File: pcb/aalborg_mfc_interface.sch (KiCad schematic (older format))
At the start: 31 parts, among them J1 DB15FV, J2 DB15FV, J3 DB15FV, P1 PWR_JACK_2.5x5.5, P2 HEADER_01X03, P3 HEADER_01X03_SHR, P4 HEADER_01X03_SHR, P5 HEADER_01X03_SHR, SW1 SPST_SERIES_M, SW2 KT_SWITCH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

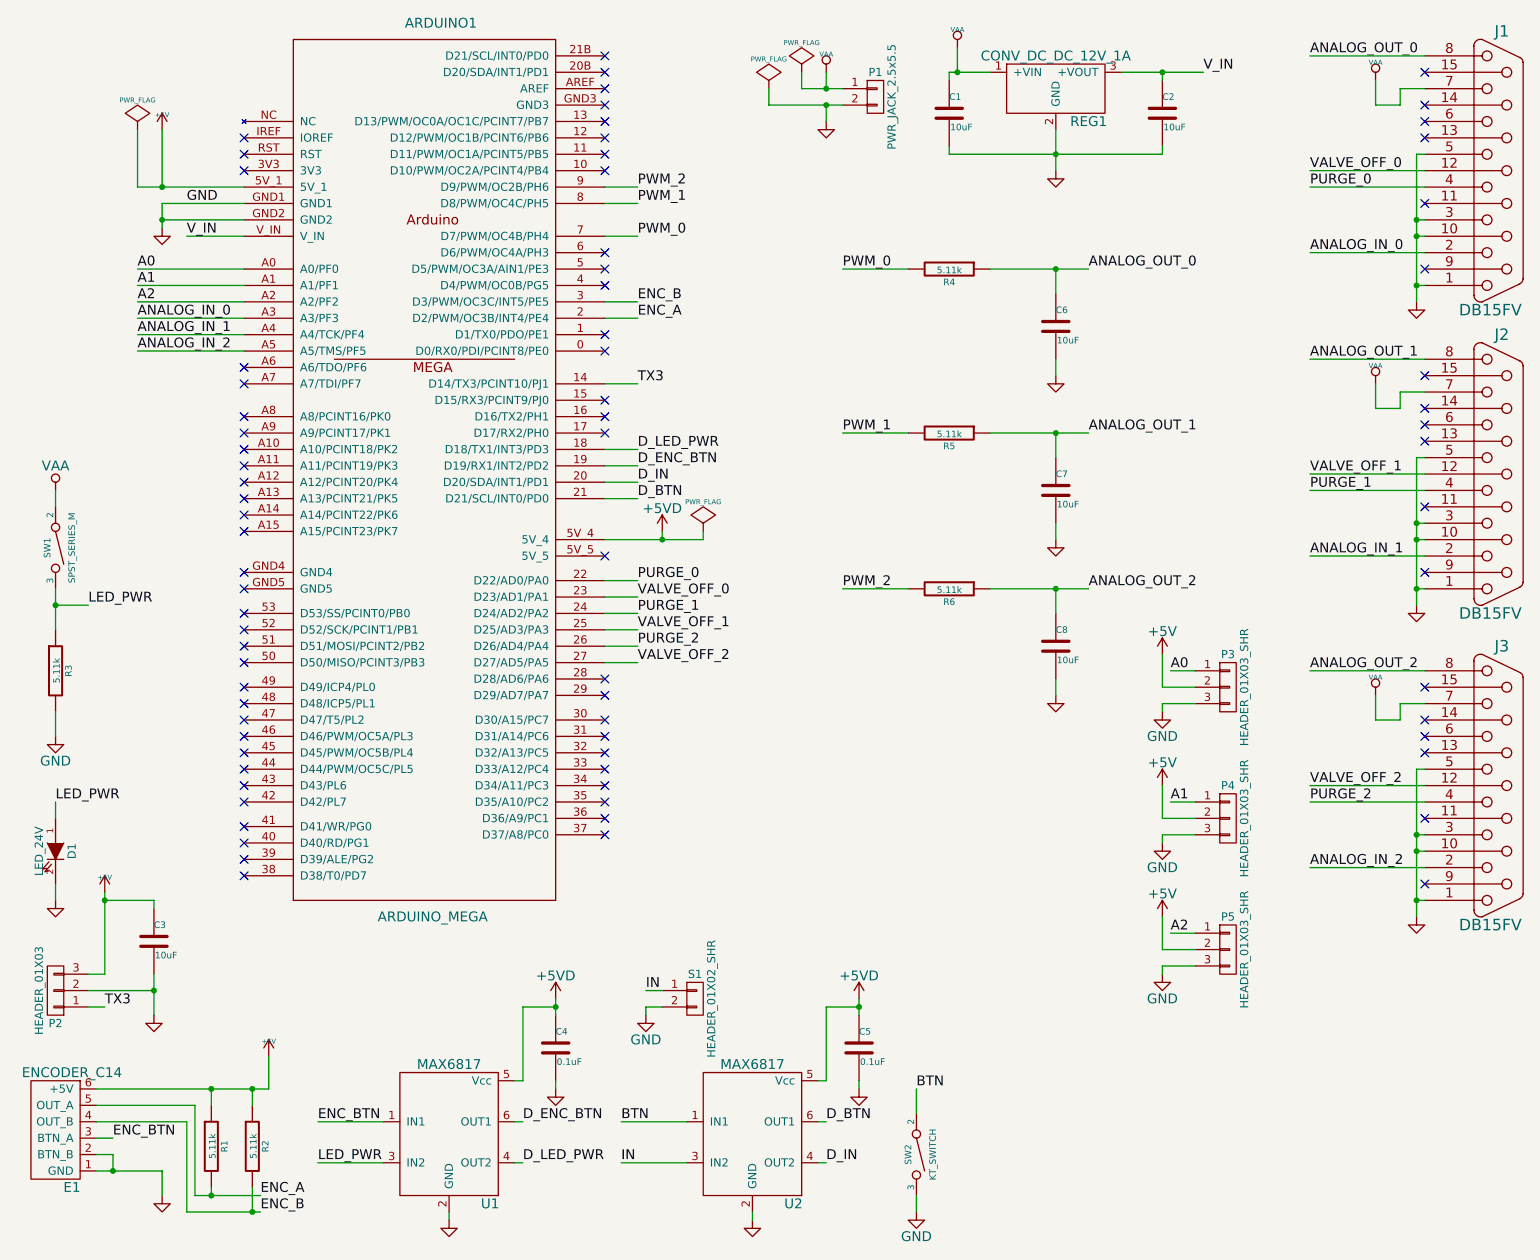
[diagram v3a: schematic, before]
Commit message: Added StandAlone frames.
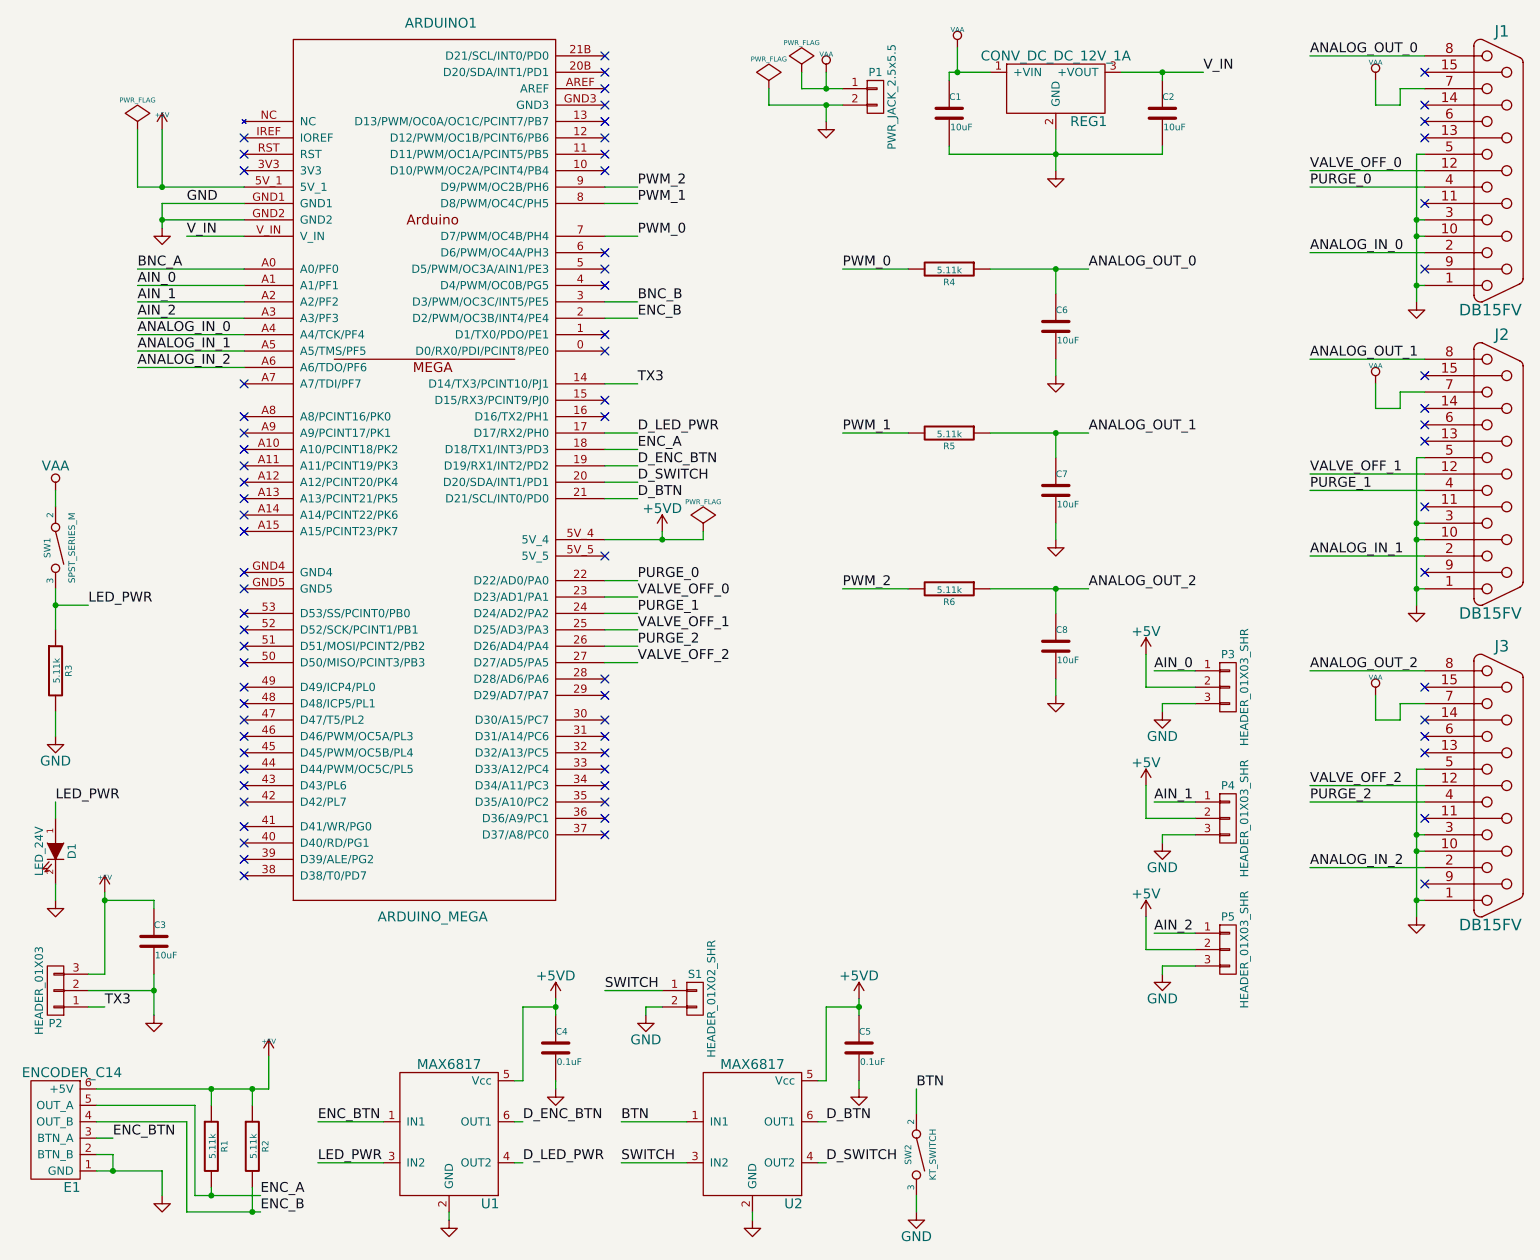
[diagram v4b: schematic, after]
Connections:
- net ANALOG_IN_0: now also ARDUINO1.A4 (A4/TCK/PF4); no longer ARDUINO1.A3 (A3/PF3)
- net ANALOG_IN_1: now also ARDUINO1.A5 (A5/TMS/PF5); no longer ARDUINO1.A4 (A4/TCK/PF4)
- net ANALOG_IN_2: now also ARDUINO1.A6 (A6/TDO/PF6); no longer ARDUINO1.A5 (A5/TMS/PF5)
- net D_LED_PWR: now also ARDUINO1.17 (D17/RX2/PH0); no longer ARDUINO1.18 (D18/TX1/INT3/PD3)
- net ENC_A: now also ARDUINO1.18 (D18/TX1/INT3/PD3); no longer ARDUINO1.2 (D2/PWM/OC3B/INT4/PE4)
- net ENC_B: now also ARDUINO1.2 (D2/PWM/OC3B/INT4/PE4); no longer ARDUINO1.3 (D3/PWM/OC3C/INT5/PE5)
- net A0 renamed AIN_0
- net AIN_0: now also ARDUINO1.A1 (A1/PF1); no longer ARDUINO1.A0 (A0/PF0)
- net A1 renamed AIN_1
- net AIN_1: now also ARDUINO1.A2 (A2/PF2); no longer ARDUINO1.A1 (A1/PF1)
- net A2 renamed AIN_2
- net AIN_2: now also ARDUINO1.A3 (A3/PF3); no longer ARDUINO1.A2 (A2/PF2)
- net D_IN renamed D_SWITCH
- net IN renamed SWITCH
- new net BNC_A: ARDUINO1.A0 (A0/PF0)
- new net BNC_B: ARDUINO1.3 (D3/PWM/OC3C/INT5/PE5)
- no-connect marks 76 -> 74
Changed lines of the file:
@@
 LIBS:valves
 LIBS:aalborg_mfc_interface
-LIBS:components
 LIBS:aalborg_mfc_interface-cache
 EELAYER 25 0
@@
 Title "aalborg_mfc_interface"
 Date ""
-Rev "1.1"
+Rev "1.2"
 Comp "Janelia"
 Comment1 ""
@@
 	1850 1750 1350 1750
 Connection ~ 1350 1750
-NoConn ~ 1850 2650
 NoConn ~ 1850 2750
 NoConn ~ 1850 2950
@@
 NoConn ~ 4050 2850
 NoConn ~ 4050 2950
-NoConn ~ 4050 3050
 NoConn ~ 4050 3800
 NoConn ~ 4050 4550
@@
 	4050 2350 4250 2350
 Text Label 4250 2350 0    60   ~ 0
-ENC_A
+ENC_B
 Wire Wire Line
 	4050 2250 4250 2250
 Text Label 4250 2250 0    60   ~ 0
-ENC_B
+BNC_B
 Wire Wire Line
 	1050 7450 1050 7550
@@
 Text Label 8350 1950 0    60   ~ 0
 ANALOG_IN_0
-Text Label 1200 2350 0    60   ~ 0
+Text Label 1200 2450 0    60   ~ 0
 ANALOG_IN_0
-Text Label 1200 2450 0    60   ~ 0
+Text Label 1200 2550 0    60   ~ 0
 ANALOG_IN_1
 Wire Wire Line
@@
 Wire Wire Line
 	4050 3150 4250 3150
-Text Label 4250 3150 0    60   ~ 0
+Text Label 4250 3050 0    60   ~ 0
 D_LED_PWR
 Text Label 700  5300 0    60   ~ 0
@@
 Wire Wire Line
 	1850 2350 1200 2350
-Text Label 1200 2550 0    60   ~ 0
+Text Label 1200 2650 0    60   ~ 0
 ANALOG_IN_2
 NoConn ~ 4050 1450
@@
 Wire Wire Line
 	1850 2550 1200 2550
-Text Label 1200 2050 0    60   ~ 0
-A0
 Text Label 1200 2150 0    60   ~ 0
-A1
+AIN_0
 Text Label 1200 2250 0    60   ~ 0
-A2
-Wire Wire Line
-	7650 4500 7500 4500
-Text Label 7500 4500 0    60   ~ 0
-A0
+AIN_1
+Text Label 1200 2350 0    60   ~ 0
+AIN_2
+Wire Wire Line
+	7650 4500 7400 4500
+Text Label 7400 4500 0    60   ~ 0
+AIN_0
 $Comp
 L +5V #PWR028
 U 1 1 54B5A3F5
-P 7450 4400
-F 0 "#PWR028" H 7450 4250 60  0001 C CNN
-F 1 "+5V" H 7450 4540 60  0000 C CNN
-F 2 "" H 7450 4400 60  0000 C CNN
-F 3 "" H 7450 4400 60  0000 C CNN
-	1    7450 4400
+P 7350 4400
+F 0 "#PWR028" H 7350 4250 60  0001 C CNN
+F 1 "+5V" H 7350 4540 60  0000 C CNN
+F 2 "" H 7350 4400 60  0000 C CNN
+F 3 "" H 7350 4400 60  0000 C CNN
+	1    7350 4400
 	1    0    0    -1
 $EndComp
@@
 $EndComp
 Wire Wire Line
-	7650 4600 7450 4600
-Wire Wire Line
-	7450 4600 7450 4400
-Wire Wire Line
 	7650 4700 7450 4700
 Wire Wire Line
 	7450 4700 7450 4750
 Wire Wire Line
-	7650 5300 7500 5300
-Text Label 7500 5300 0    60   ~ 0
-A1
+	7650 5300 7400 5300
+Text Label 7400 5300 0    60   ~ 0
+AIN_1
 $Comp
 L +5V #PWR030
 U 1 1 54B5A9BF
-P 7450 5200
-F 0 "#PWR030" H 7450 5050 60  0001 C CNN
-F 1 "+5V" H 7450 5340 60  0000 C CNN
-F 2 "" H 7450 5200 60  0000 C CNN
-F 3 "" H 7450 5200 60  0000 C CNN
-	1    7450 5200
+P 7350 5200
+F 0 "#PWR030" H 7350 5050 60  0001 C CNN
+F 1 "+5V" H 7350 5340 60  0000 C CNN
+F 2 "" H 7350 5200 60  0000 C CNN
+F 3 "" H 7350 5200 60  0000 C CNN
+	1    7350 5200
 	1    0    0    -1
 $EndComp
@@
 $EndComp
 Wire Wire Line
-	7650 5400 7450 5400
-Wire Wire Line
-	7450 5400 7450 5200
-Wire Wire Line
 	7650 5500 7450 5500
 Wire Wire Line
 	7450 5500 7450 5550
 Wire Wire Line
-	7650 6100 7500 6100
-Text Label 7500 6100 0    60   ~ 0
-A2
+	7650 6100 7400 6100
+Text Label 7400 6100 0    60   ~ 0
+AIN_2
 $Comp
 L +5V #PWR032
 U 1 1 54B5AB98
-P 7450 6000
-F 0 "#PWR032" H 7450 5850 60  0001 C CNN
-F 1 "+5V" H 7450 6140 60  0000 C CNN
-F 2 "" H 7450 6000 60  0000 C CNN
-F 3 "" H 7450 6000 60  0000 C CNN
-	1    7450 6000
+P 7350 6000
+F 0 "#PWR032" H 7350 5850 60  0001 C CNN
+F 1 "+5V" H 7350 6140 60  0000 C CNN
+F 2 "" H 7350 6000 60  0000 C CNN
+F 3 "" H 7350 6000 60  0000 C CNN
+	1    7350 6000
 	1    0    0    -1
 $EndComp
@@
 	1    0    0    -1
 $EndComp
-Wire Wire Line
-	7650 6200 7450 6200
-Wire Wire Line
-	7450 6200 7450 6000
 Wire Wire Line
 	7650 6300 7450 6300
@@
 	4550 7500 4150 7500
 Text Label 4150 7500 0    60   ~ 0
-IN
+SWITCH
 Wire Wire Line
 	5350 7500 5400 7500
 Text Label 5400 7500 0    60   ~ 0
-D_IN
+D_SWITCH
 $Comp
 L +5VD #PWR039
@@
 Connection ~ 5600 6550
 Wire Wire Line
-	4400 6450 4300 6450
-Text Label 4300 6450 0    60   ~ 0
-IN
+	4400 6450 4050 6450
+Text Label 4050 6450 0    60   ~ 0
+SWITCH
 $Comp
 L GND #PWR040
@@
 D_BTN
 Text Label 4250 3350 0    60   ~ 0
-D_IN
+D_SWITCH
 $Comp
 L GND #PWR041
@@
 	1    0    0    -1
 $EndComp
+Wire Wire Line
+	4050 3050 4250 3050
+Text Label 4250 3150 0    60   ~ 0
+ENC_A
+Wire Wire Line
+	1850 2650 1200 2650
+Text Label 1200 2050 0    60   ~ 0
+BNC_A
+Wire Wire Line
+	7350 4400 7350 4600
+Wire Wire Line
+	7350 4600 7650 4600
+Wire Wire Line
+	7350 5200 7350 5400
+Wire Wire Line
+	7350 5400 7650 5400
+Wire Wire Line
+	7350 6000 7350 6200
+Wire Wire Line
+	7350 6200 7650 6200
 $EndSCHEMATC

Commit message: Finished pcb v1.2.
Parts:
- added P3: BNC_DOUBLE_RA, aalborg_mfc_interface:BNC_DOUBLE, symbol BNC_DOUBLE_RA
- renumbered P3 to P4, P4 to P5, P5 to P6
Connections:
- net BNC_A: now also P3.1 (P1)
- net BNC_B: now also P3.3 (P3)
- net GND: now also P3.2 (P2), P3.4 (P4)
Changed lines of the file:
@@
 	1200 1200 1200 1550
 Wire Wire Line
-	1200 1550 1350 1550
-Wire Wire Line
-	1350 1550 1850 1550
+	1200 1550 1850 1550
 Wire Wire Line
 	1350 1200 1350 1550
@@
 	1850 1650 1350 1650
 Wire Wire Line
-	1350 1650 1350 1750
-Wire Wire Line
-	1350 1750 1350 1800
+	1350 1650 1350 1800
 Wire Wire Line
 	1850 1750 1350 1750
@@
 $EndComp
 Wire Wire Line
-	5250 950  5400 950
-Wire Wire Line
-	5400 950  5500 950
+	5250 950  5500 950
 Wire Wire Line
 	5250 950  5250 850
@@
 Connection ~ 5400 950
 Wire Wire Line
-	5050 1050 5400 1050
-Wire Wire Line
-	5400 1050 5500 1050
+	5050 1050 5500 1050
 Wire Wire Line
 	5050 1050 5050 950
@@
 $EndComp
 Wire Wire Line
-	1300 6350 1300 6450
-Wire Wire Line
-	1300 6450 1300 6600
+	1300 6350 1300 6600
 Wire Wire Line
 	900  6450 1300 6450
@@
 	1300 5900 1000 5900
 Wire Wire Line
-	1000 5850 1000 5900
-Wire Wire Line
-	1000 5900 1000 6350
+	1000 5850 1000 6350
 Wire Wire Line
 	1000 6350 900  6350
@@
 $EndComp
 Wire Wire Line
-	6800 1200 6800 1350
-Wire Wire Line
-	6800 1350 6800 1450
+	6800 1200 6800 1450
 Wire Wire Line
 	6150 1300 6150 1350
 Wire Wire Line
-	6150 1350 6800 1350
-Wire Wire Line
-	6800 1350 7450 1350
+	6150 1350 7450 1350
 Connection ~ 6800 1350
 Wire Wire Line
@@
 	6150 900  6150 850
 Wire Wire Line
-	6150 850  6200 850
-Wire Wire Line
-	6200 850  6400 850
-Wire Wire Line
-	7200 850  7450 850
-Wire Wire Line
-	7450 850  7700 850
+	6150 850  6400 850
+Wire Wire Line
+	7200 850  7700 850
 Wire Wire Line
 	7450 900  7450 850
@@
 $EndComp
 Wire Wire Line
-	950  7550 1050 7550
-Wire Wire Line
-	1050 7550 1350 7550
+	950  7550 1350 7550
 Wire Wire Line
 	1350 7550 1350 7700
@@
 $EndComp
 Wire Wire Line
-	950  7050 1650 7050
-Wire Wire Line
-	1650 7050 1900 7050
-Wire Wire Line
-	1900 7050 2000 7050
+	950  7050 2000 7050
 Wire Wire Line
 	2000 7050 2000 6850
@@
 	1550 7150 1550 7700
 Wire Wire Line
-	1550 7700 1650 7700
-Wire Wire Line
-	1650 7700 1950 7700
+	1550 7700 1950 7700
 Wire Wire Line
 	950  7250 1500 7250
@@
 	1500 7250 1500 7800
 Wire Wire Line
-	1500 7800 1900 7800
-Wire Wire Line
-	1900 7800 1950 7800
+	1500 7800 1950 7800
 Text Label 1050 7350 0    60   ~ 0
 ENC_BTN
@@
 	3750 7000 3750 7050
 Wire Wire Line
-	3750 6500 3750 6550
-Wire Wire Line
-	3750 6550 3750 6600
+	3750 6500 3750 6600
 Wire Wire Line
 	4050 3250 4250 3250
@@
 	9050 1350 9000 1350
 Wire Wire Line
-	9000 1350 9000 1750
-Wire Wire Line
-	9000 1750 9000 1850
-Wire Wire Line
-	9000 1850 9000 2150
-Wire Wire Line
-	9000 2150 9000 2250
+	9000 1350 9000 2250
 Wire Wire Line
 	9050 2150 9000 2150
@@
 	6800 2600 6800 2700
 Wire Wire Line
-	6400 2050 6800 2050
-Wire Wire Line
-	6800 2050 7000 2050
+	6400 2050 7000 2050
 Wire Wire Line
 	6800 2200 6800 2050
@@
 	6800 3600 6800 3700
 Wire Wire Line
-	6400 3050 6800 3050
-Wire Wire Line
-	6800 3050 7000 3050
+	6400 3050 7000 3050
 Wire Wire Line
 	6800 3200 6800 3050
@@
 	9050 3200 9000 3200
 Wire Wire Line
-	9000 3200 9000 3600
-Wire Wire Line
-	9000 3600 9000 3700
-Wire Wire Line
-	9000 3700 9000 4000
-Wire Wire Line
-	9000 4000 9000 4100
+	9000 3200 9000 4100
 Wire Wire Line
 	9050 4000 9000 4000
@@
 $EndComp
 Wire Wire Line
-	700  4000 700  4100
-Wire Wire Line
-	700  4100 700  4250
+	700  4000 700  4250
 Wire Wire Line
 	700  4750 700  4900
@@
 	9050 5100 9000 5100
 Wire Wire Line
-	9000 5100 9000 5500
-Wire Wire Line
-	9000 5500 9000 5600
-Wire Wire Line
-	9000 5600 9000 5900
-Wire Wire Line
-	9000 5900 9000 6000
+	9000 5100 9000 6000
 Wire Wire Line
 	9050 5900 9000 5900
@@
 	6800 4550 6800 4650
 Wire Wire Line
-	6400 4000 6800 4000
-Wire Wire Line
-	6800 4000 7000 4000
+	6400 4000 7000 4000
 Wire Wire Line
 	6800 4150 6800 4000
@@
 $EndComp
 Wire Wire Line
-	4050 3700 4400 3700
-Wire Wire Line
-	4400 3700 4650 3700
+	4050 3700 4650 3700
 Wire Wire Line
 	4400 3700 4400 3650
@@
 	5600 7000 5600 7050
 Wire Wire Line
-	5600 6500 5600 6550
-Wire Wire Line
-	5600 6550 5600 6600
+	5600 6500 5600 6600
 $Comp
 L 0.1uF C5
@@
 $EndComp
 $Comp
-L HEADER_01X03_SHR P3
+L HEADER_01X03_SHR P4
 U 1 1 54B9D7EF
 P 7850 4600
-F 0 "P3" H 7850 4800 50  0000 C CNN
+F 0 "P4" H 7850 4800 50  0000 C CNN
 F 1 "HEADER_01X03_SHR" V 7950 4600 50  0000 C CNN
 F 2 "aalborg_mfc_interface:Header_Shrouded_3_Pin" H 7750 4700 60  0001 C CNN
@@
 $EndComp
 $Comp
-L HEADER_01X03_SHR P4
+L HEADER_01X03_SHR P5
 U 1 1 54B9D9D9
 P 7850 5400
-F 0 "P4" H 7850 5600 50  0000 C CNN
+F 0 "P5" H 7850 5600 50  0000 C CNN
 F 1 "HEADER_01X03_SHR" V 7950 5400 50  0000 C CNN
 F 2 "aalborg_mfc_interface:Header_Shrouded_3_Pin" H 7750 5500 60  0001 C CNN
@@
 $EndComp
 $Comp
-L HEADER_01X03_SHR P5
+L HEADER_01X03_SHR P6
 U 1 1 54B9DA07
 P 7850 6200
-F 0 "P5" H 7850 6400 50  0000 C CNN
+F 0 "P6" H 7850 6400 50  0000 C CNN
 F 1 "HEADER_01X03_SHR" V 7950 6200 50  0000 C CNN
 F 2 "aalborg_mfc_interface:Header_Shrouded_3_Pin" H 7750 6300 60  0001 C CNN
@@
 Wire Wire Line
 	7350 6200 7650 6200
+$Comp
+L BNC_DOUBLE_RA P3
+U 1 1 54EB8C82
+P 2550 6350
+F 0 "P3" H 2550 6500 50  0000 C CNN
+F 1 "BNC_DOUBLE_RA" H 2550 6200 50  0000 C CNN
+F 2 "aalborg_mfc_interface:BNC_DOUBLE" H 2550 5150 60  0001 C CNN
+F 3 "" H 2550 5150 60  0000 C CNN
+F 4 "digikey" H 2650 6600 60  0001 C CNN "Vendor"
+F 5 "ACX1655-ND" H 2750 6700 60  0001 C CNN "PartNumber"
+F 6 "CONN BNC JACK R/A 75 OHM PCB" H 2850 6800 60  0001 C CNN "Description"
+	1    2550 6350
+	1    0    0    -1
+$EndComp
+$Comp
+L GND #PWR042
+U 1 1 54EB8D56
+P 2950 6450
+F 0 "#PWR042" H 2950 6200 60  0001 C CNN
+F 1 "GND" H 2950 6300 60  0000 C CNN
+F 2 "" H 2950 6450 60  0000 C CNN
+F 3 "" H 2950 6450 60  0000 C CNN
+	1    2950 6450
+	1    0    0    -1
+$EndComp
+Wire Wire Line
+	2800 6300 2950 6300
+Wire Wire Line
+	2950 6300 2950 6450
+Wire Wire Line
+	2800 6400 2950 6400
+Connection ~ 2950 6400
+Wire Wire Line
+	2300 6300 1950 6300
+Wire Wire Line
+	2300 6400 1950 6400
+Text Label 1950 6300 0    60   ~ 0
+BNC_A
+Text Label 1950 6400 0    60   ~ 0
+BNC_B
 $EndSCHEMATC
